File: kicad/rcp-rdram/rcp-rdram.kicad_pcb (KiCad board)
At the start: 4 copper layers, 47.1 x 49.7 mm, 35 parts, among them P1 RDRAM-EDGE, U11 RDRAM18-NUS, U11-2 RDRAM18-NUS, U14 RDRAM18-NUS, U14-2 RDRAM18-NUS, U15 8330, X2 14.705MHz

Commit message: 4 layers WIP
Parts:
- moved CRD3 23.0 mm to (28.2, 28.1)
- moved CRD4 23.0 mm to (28.2, 45.7)
- moved C132 7.65 mm to (42.0, 33.0), turned to 90 degrees
- moved C133 1.59 mm to (41.6, 28.0), turned to 180 degrees
- moved CRD2 0.95 mm to (50.8, 48.3), turned to 270 degrees
- moved CRD1 0.42 mm to (50.8, 65.9)
- moved JP1 0.41 mm to (41.8, 27.4)
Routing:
- net +3V3: track 22.4 -> 46.4 mm, vias 4 -> 14
- net Net-(JP1-Pad2): track 0.00 -> 19.2 mm
- net Net-(U11-2-Pad20): track 0.00 -> 18.1 mm
- net GND: track 22.0 -> 39.6 mm, vias 9 -> 27
- net /VTERM: track 69.8 -> 82.4 mm, vias 36 -> 43
- net /VREF: track 54.7 -> 66.5 mm, vias 6 -> 9
- net /ENABLE: track 13.5 -> 18.5 mm
- net Net-(JP1-Pad1): track 0.00 -> 2.86 mm, vias 0 -> 1

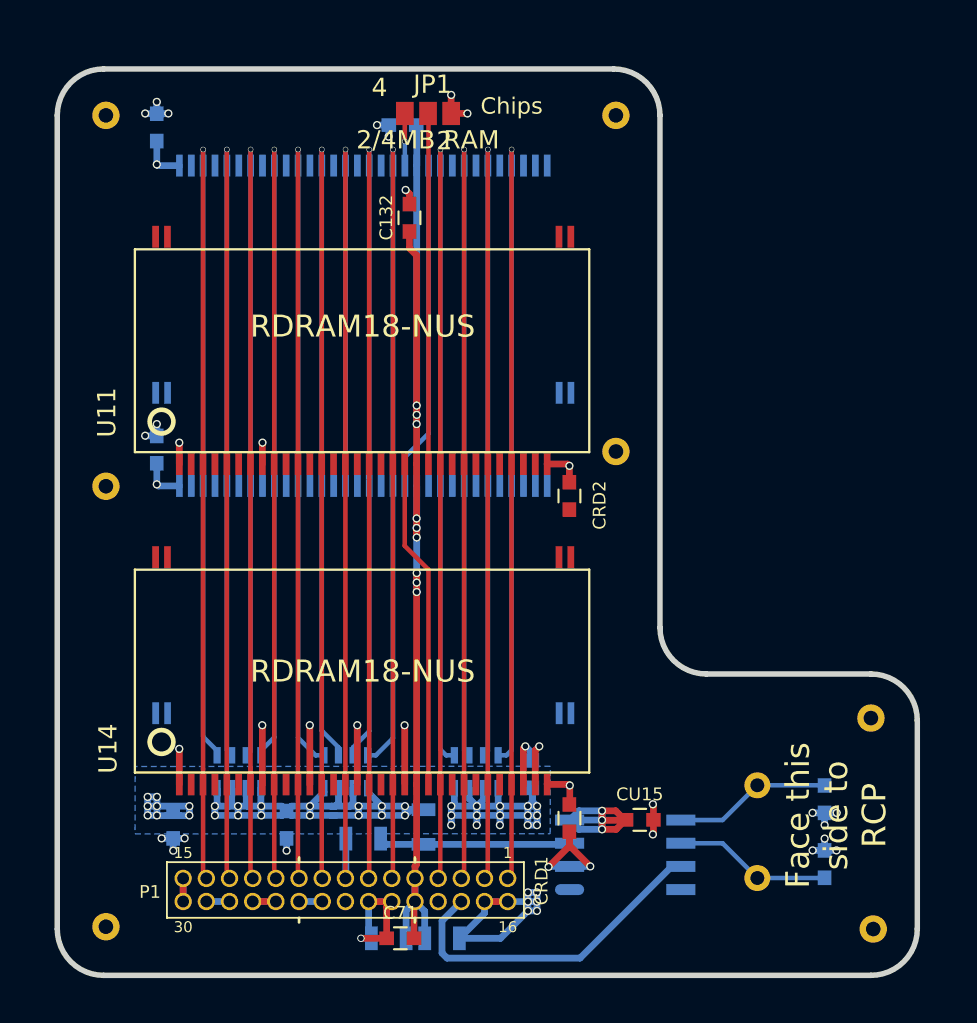
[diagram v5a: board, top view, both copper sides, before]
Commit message: Finished 4 layer board
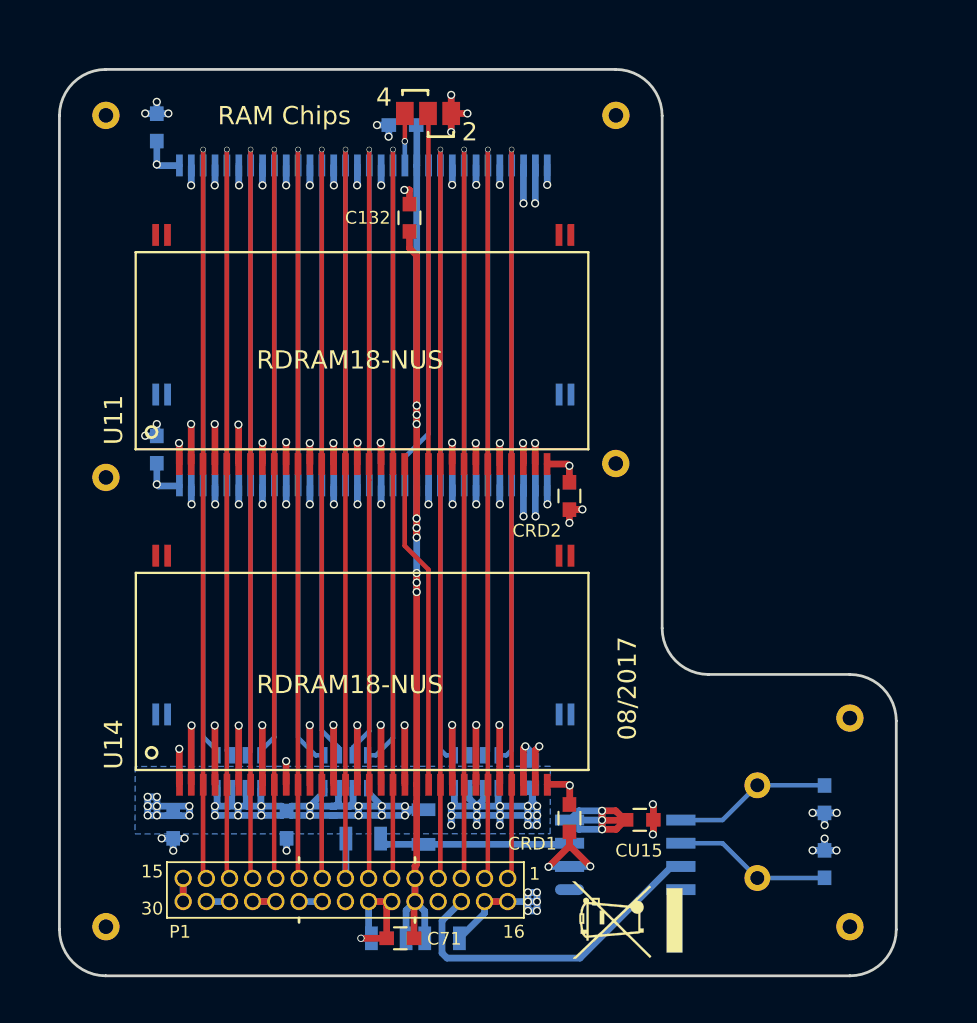
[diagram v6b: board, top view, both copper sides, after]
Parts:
- added REF***: KiCad-Logo2_6mm_SilkScreen, Symbols:WEEE-Logo_4.2x6mm_SilkScreen, F.Cu at (54.0, 71.5)
- moved U14 13.3 mm to (51.9, 63.4), turned to 90 degrees
- moved U11-2 13.3 mm to (51.9, 48.4), turned to 270 degrees
- moved U14-2 13.3 mm to (51.9, 30.9), turned to 270 degrees
- moved U11 13.3 mm to (51.9, 45.8), turned to 90 degrees
- moved REF** 1.28 mm to (66.2, 72.0)
- moved REF** 0.66 mm to (53.3, 46.5)
- moved REF** 0.48 mm to (25.4, 47.3)
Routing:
- net GND: track 39.6 -> 112.6 mm, vias 27 -> 73
- net +3V3: track 46.4 -> 57.0 mm, vias 14 -> 24
- net /VTERM: track 82.4 -> 78.0 mm
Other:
- board size 47.1 x 49.7 mm -> 45.8 x 49.7 mm
- net class Default: via_dia 0.3 -> 0.35
- board text added: "08/2017"
- board text added: "1"
- board text added: "Designed by dmkfasi"
- board text added: "RAM Chips"
- board text removed: "Chips"
- board text removed: "Face this side to RCP"
- board text removed: "Top side"
